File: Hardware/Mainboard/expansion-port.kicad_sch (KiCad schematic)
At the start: 1 part, among them J2 Conn_02x10_Odd_Even

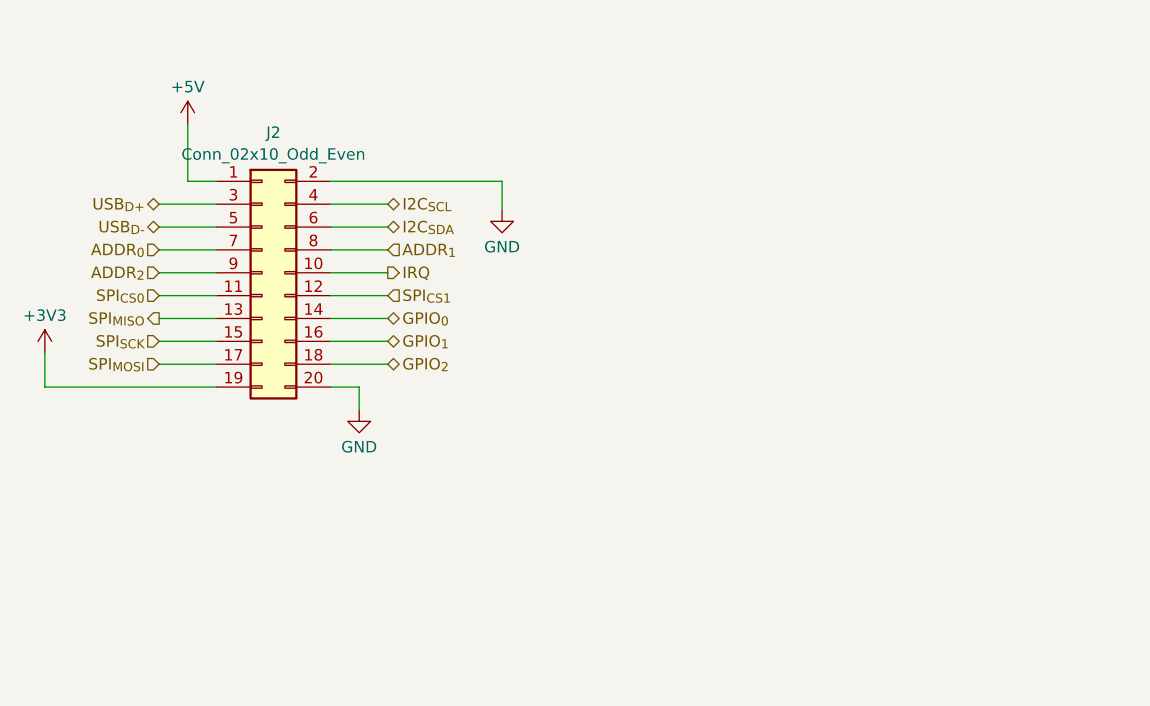
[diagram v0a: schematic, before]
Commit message: Adds more work on the mainboard schematic
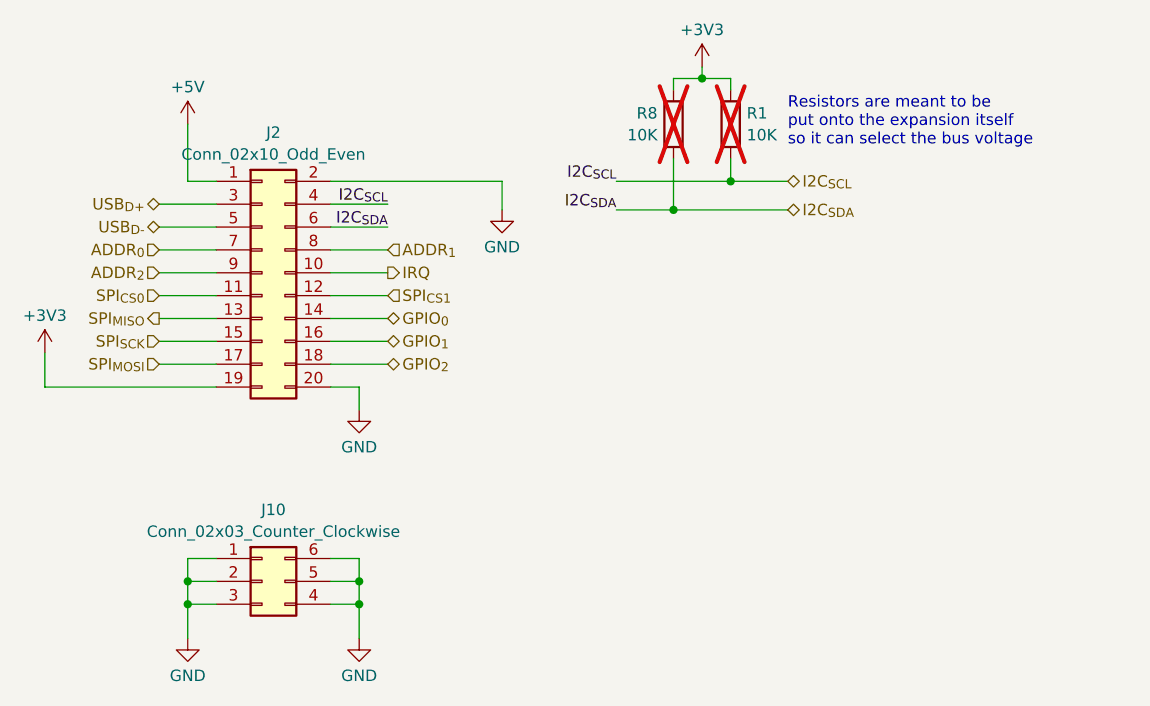
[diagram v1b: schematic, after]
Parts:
- added J10: Conn_02x03_Counter_Clockwise, Connector_PinSocket_2.54mm:PinSocket_2x03_P2.54mm_Vertical, symbol Connector_Generic:Conn_02x03_Counter_Clockwise
- added R1, R8: 10K, Resistor_SMD:R_0603_1608Metric_Pad0.98x0.95mm_HandSolder, symbol Device:R
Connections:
- net +3V3: now also R1.1, R8.1
- net GND: now also J10.1 (Pin_1), J10.2 (Pin_2), J10.3 (Pin_3), J10.4 (Pin_4), J10.5 (Pin_5), J10.6 (Pin_6)
- net I2C_{SCL}: now also R1.2
- net I2C_{SDA}: now also R8.2
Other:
- note added: "Resistors are meant to be put onto the expansion itself so it can select the bus voltage"

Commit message: Adds RP2350 Stamp XL and dummy expansion board
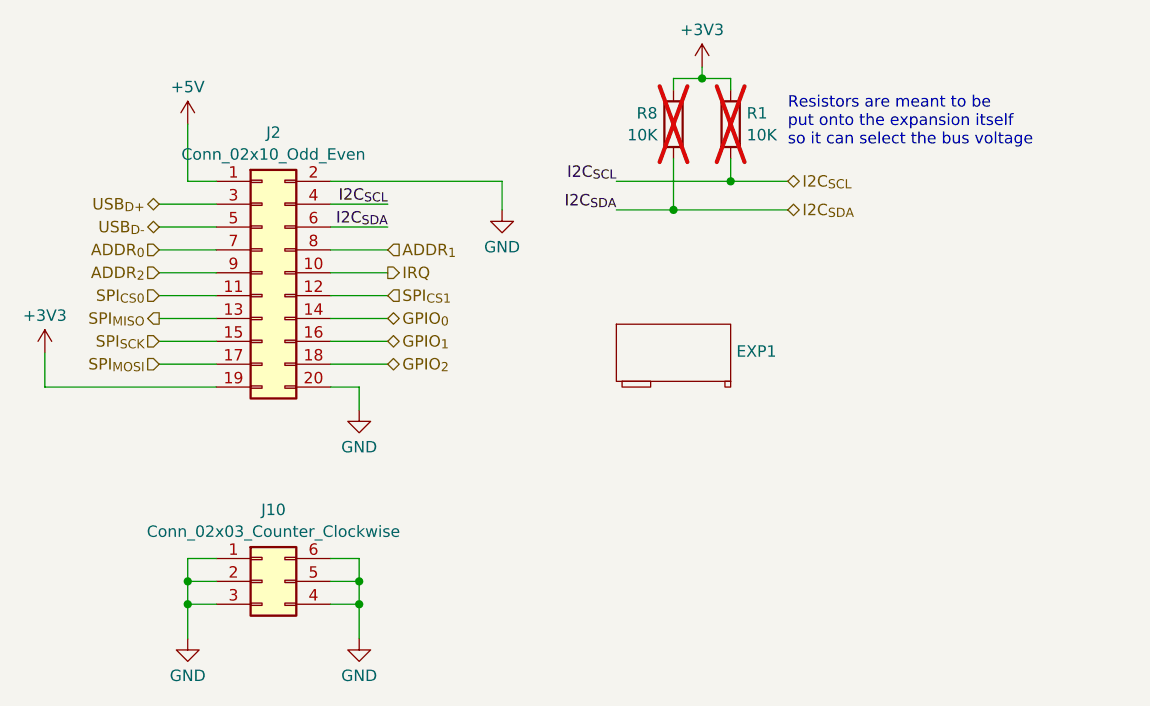
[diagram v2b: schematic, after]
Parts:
- added EXP1: ~, Home Computer:Expansion Card Preview, symbol Home Computer:Ashet_Expansion_Card

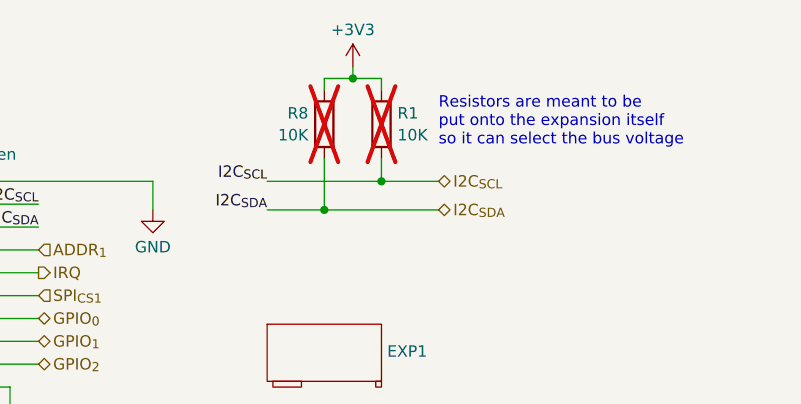
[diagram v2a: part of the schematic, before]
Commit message: Adds pull-ups and irq controller to expansion subsystem
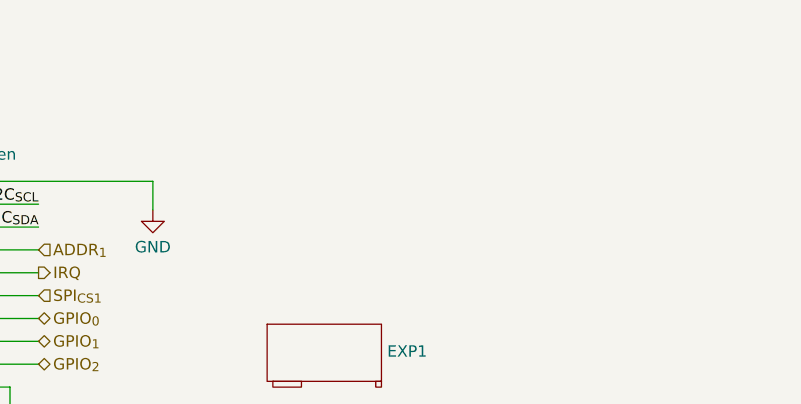
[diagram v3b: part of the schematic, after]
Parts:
- removed R1, R8: 10K, Resistor_SMD:R_0603_1608Metric_Pad0.98x0.95mm_HandSolder, symbol Device:R
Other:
- note removed: "Resistors are meant to be put onto the expansion itself so it can select the bus voltage"

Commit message: More work on the motherboard
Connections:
- net SPI_{MISO}: now also J2.17 (Pin_17); no longer J2.13 (Pin_13)
- net SPI_{MOSI}: now also J2.15 (Pin_15); no longer J2.17 (Pin_17)
- net SPI_{SCK}: now also J2.13 (Pin_13); no longer J2.15 (Pin_15)
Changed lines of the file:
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@@
 	(hierarchical_label "SPI_{MOSI}"
 		(shape input)
-		(at 57.15 64.77 180)
+		(at 57.15 62.23 180)
 		(fields_autoplaced yes)
 		(effects
@@
 	(hierarchical_label "SPI_{SCK}"
 		(shape input)
-		(at 57.15 62.23 180)
+		(at 57.15 59.69 180)
 		(fields_autoplaced yes)
 		(effects
@@
 	(hierarchical_label "SPI_{MISO}"
 		(shape output)
-		(at 57.15 59.69 180)
+		(at 57.15 64.77 180)
 		(fields_autoplaced yes)
 		(effects
